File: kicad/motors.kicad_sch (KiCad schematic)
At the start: 33 parts, among them U1 DRV8251A, U15 DRV8251A, U16 DRV8251A, U17 DRV8251A, U2 DRV8251A, U3 DRV8251A

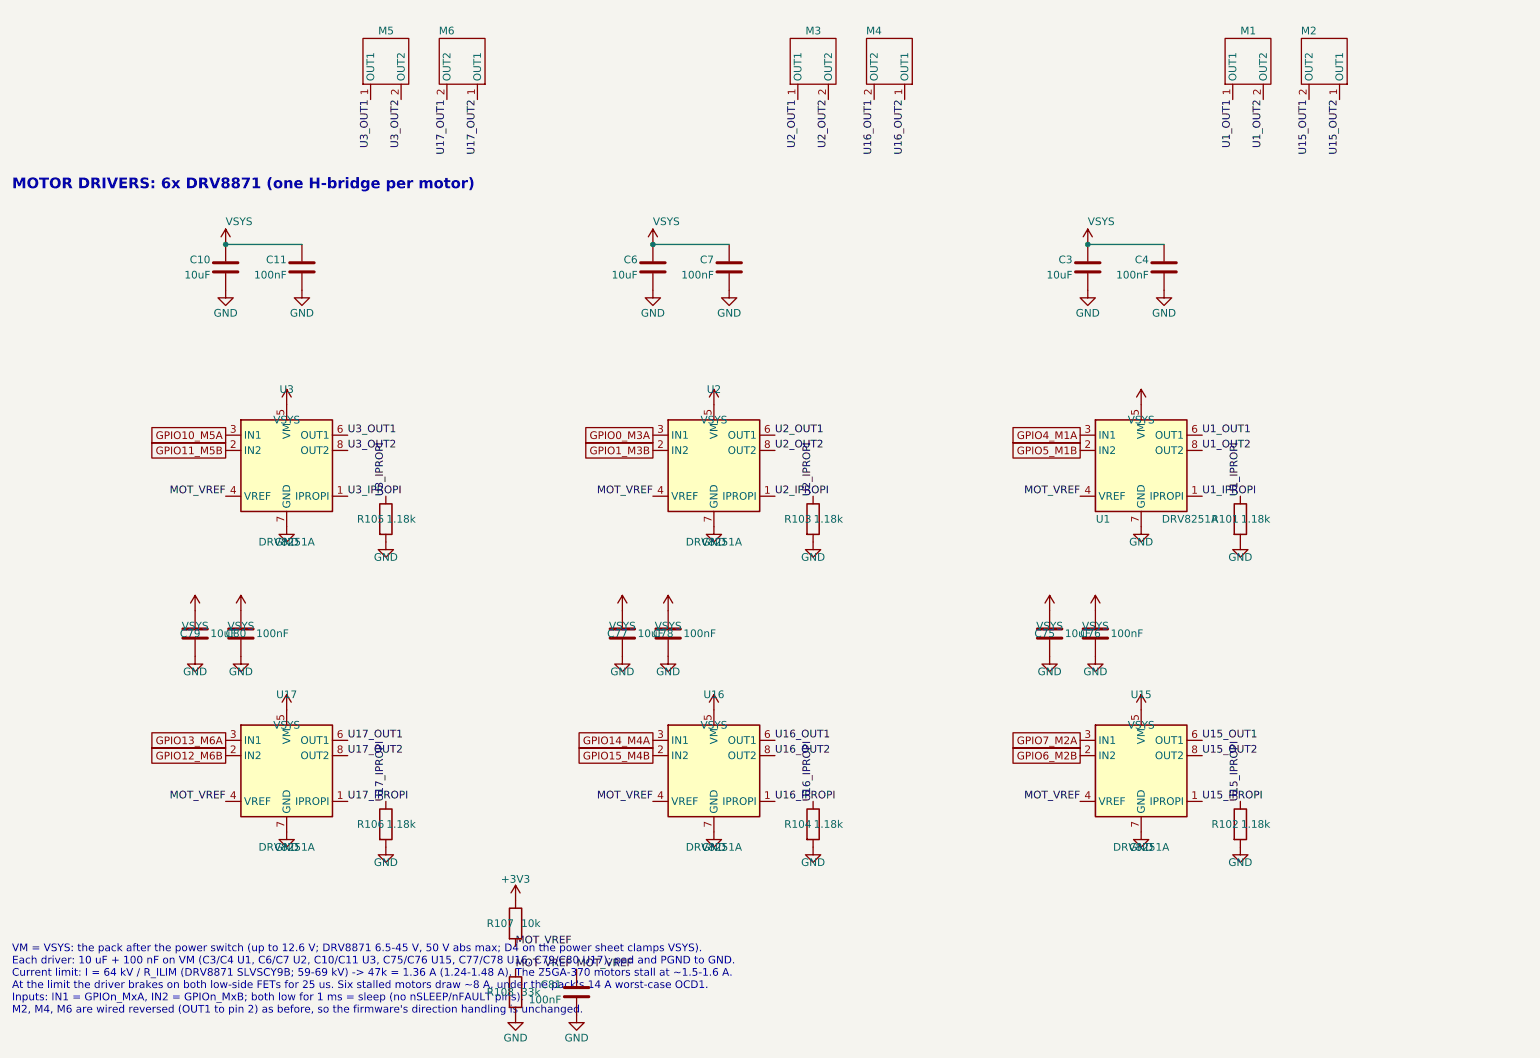
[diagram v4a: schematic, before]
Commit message: Fill in LCSC numbers, swap to stocked parts, tidy the new schematic parts
- LCSC numbers from JLC's 2026-10-19 in-stock catalog for every new part
  except the DRV8251A, which JLC doesn't stock (Global Sourcing or consign).
- 2S protector S-8252AAH -> HY2120-LB (C168778): pin-for-pin the same,
  OV 4.25 V / UV 2.80 V, stocked at JLC. R94 trip recovery still holds.
- IPROPI R101-R106 1.18k (2,341 in stock) -> 1.2k preferred (C25862),
  so the motor limit is 1.34 A.
- Fix the 2S pack board's footprint-symbol links (paths were dropped in
  the previous commit); both boards now link every footprint correctly.
- Move the VREF divider and the balancer block into clear space and
  rewrite the stale DRV8871/BQ7791501 notes on the motor and 2S sheets.

Co-Authored-By: Claude Opus 5.5 <noreply@anthropic.com>
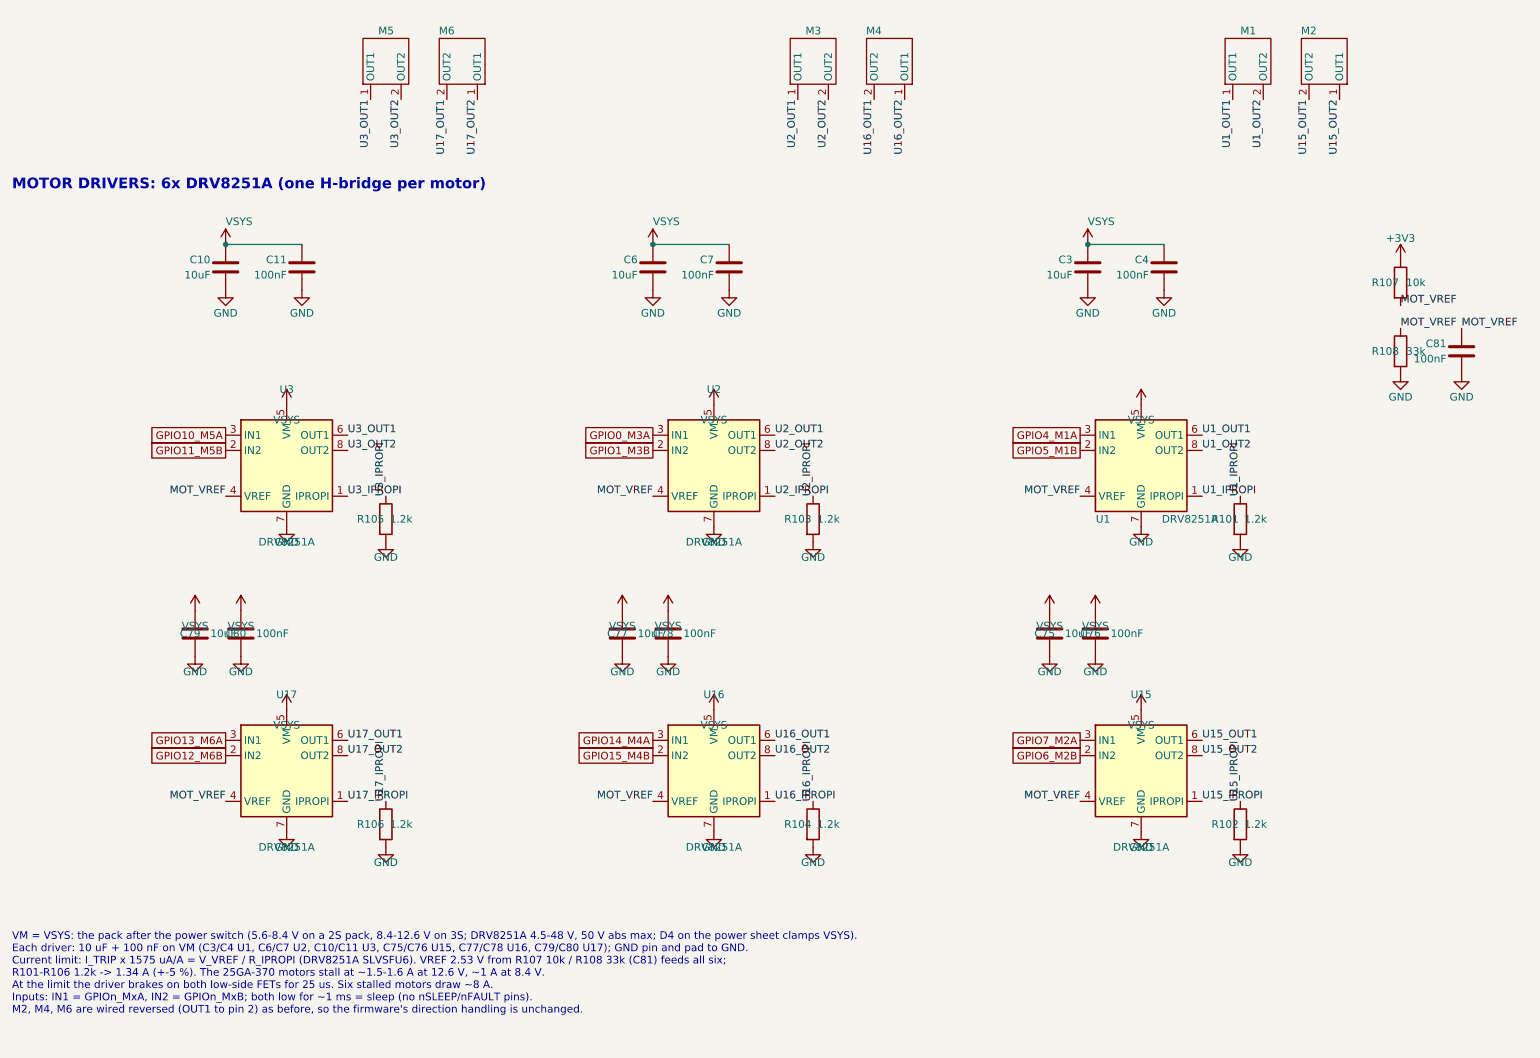
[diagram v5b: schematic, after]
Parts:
- R101, R102, R103, R104, R105, R106: value 1.18k -> 1.2k; LCSC Part # (none) -> C25862; MPN 0402WGF1181TCE -> 0402WGF1201TCE
- R108: LCSC Part # (none) -> C25779
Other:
- note added: "MOTOR DRIVERS: 6x DRV8251A (one H-bridge per motor)"
- note added: "VM = VSYS: the pack after the power switch (5.6-8.4 V on a 2S pack, 8.4-12.6 V on 3S; DRV8251A 4.5-48 V, 50 V abs max; D4 on the power sheet clamps VSYS). Each driver: 10 uF + 100 nF on VM (C3/C4 U1, C6/C7 U2, C10/C11 U3, C75/C76 U15, C77/C78 U16, C79/C80 U17); GND pin and pad to GND. Current limit: I_TRIP x 1575 uA/A = V_VREF / R_IPROPI (DRV8251A SLVSFU6). VREF 2.53 V from R107 10k / R108 33k (C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"
- note removed: "MOTOR DRIVERS: 6x DRV8871 (one H-bridge per motor)"
- note removed: "VM = VSYS: the pack after the power switch (up to 12.6 V; DRV8871 6.5-45 V, 50 V abs max; D4 on the power sheet clamps VSYS). Each driver: 10 uF + 100 nF on VM (C3/C4 U1, C6/C7 U2, C10/C11 U3, C75/C76 U15, C77/C78 U16, C79/C80 U17); pad and PGND to GND. Current limit: I = 64 kV / R_ILIM (DRV8871 SLVSCY9B; 59-69 kV) -> 47k = 1.36 A (1.24-1.48 A). The 25GA-370 motors stall at ~1.5-1.6 A. At the lim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"
- moved on the sheet: C81, R107, R108

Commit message: Give the six DRV8251As LCSC C5218844 so JLC places them
The genuine TI DRV8251ADDAR is stocked at LCSC as C5218844, so the motor
drivers no longer need Global Sourcing or consigning. fab.py now puts
U1-U3 and U15-U17 in the JLC BOM and CPL with nothing flagged.

Co-Authored-By: Claude Opus 5.5 <noreply@anthropic.com>
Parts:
- U1, U15, U16, U17, U2, U3: LCSC Part # (none) -> C5218844
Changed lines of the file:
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@@
       (effects (font (size 1.27 1.27)) (hide yes))
     )
-    (property "LCSC Part #" "" (at 215.9 88.9 0)
+    (property "LCSC Part #" "C5218844" (at 215.9 88.9 0)
       (effects (font (size 1.27 1.27)) (hide yes))
     )
@@
       (effects (font (size 1.27 1.27)) (hide yes))
     )
-    (property "LCSC Part #" "" (at 215.9 139.7 0)
+    (property "LCSC Part #" "C5218844" (at 215.9 139.7 0)
       (effects (font (size 1.27 1.27)) (hide yes))
     )
@@
       (effects (font (size 1.27 1.27)) (hide yes))
     )
-    (property "LCSC Part #" "" (at 144.78 88.9 0)
+    (property "LCSC Part #" "C5218844" (at 144.78 88.9 0)
       (effects (font (size 1.27 1.27)) (hide yes))
     )
@@
       (effects (font (size 1.27 1.27)) (hide yes))
     )
-    (property "LCSC Part #" "" (at 144.78 139.7 0)
+    (property "LCSC Part #" "C5218844" (at 144.78 139.7 0)
       (effects (font (size 1.27 1.27)) (hide yes))
     )
@@
       (effects (font (size 1.27 1.27)) (hide yes))
     )
-    (property "LCSC Part #" "" (at 73.66 88.9 0)
+    (property "LCSC Part #" "C5218844" (at 73.66 88.9 0)
       (effects (font (size 1.27 1.27)) (hide yes))
     )
@@
       (effects (font (size 1.27 1.27)) (hide yes))
     )
-    (property "LCSC Part #" "" (at 73.66 139.7 0)
-      (effects (font (size 1.27 1.27)) (hide yes))
-    )
+    (property "LCSC Part #" "C5218844" (at 73.66 139.7 0)
+      (effects (font (size 1.27 1.27)) (hide yes))
+    )

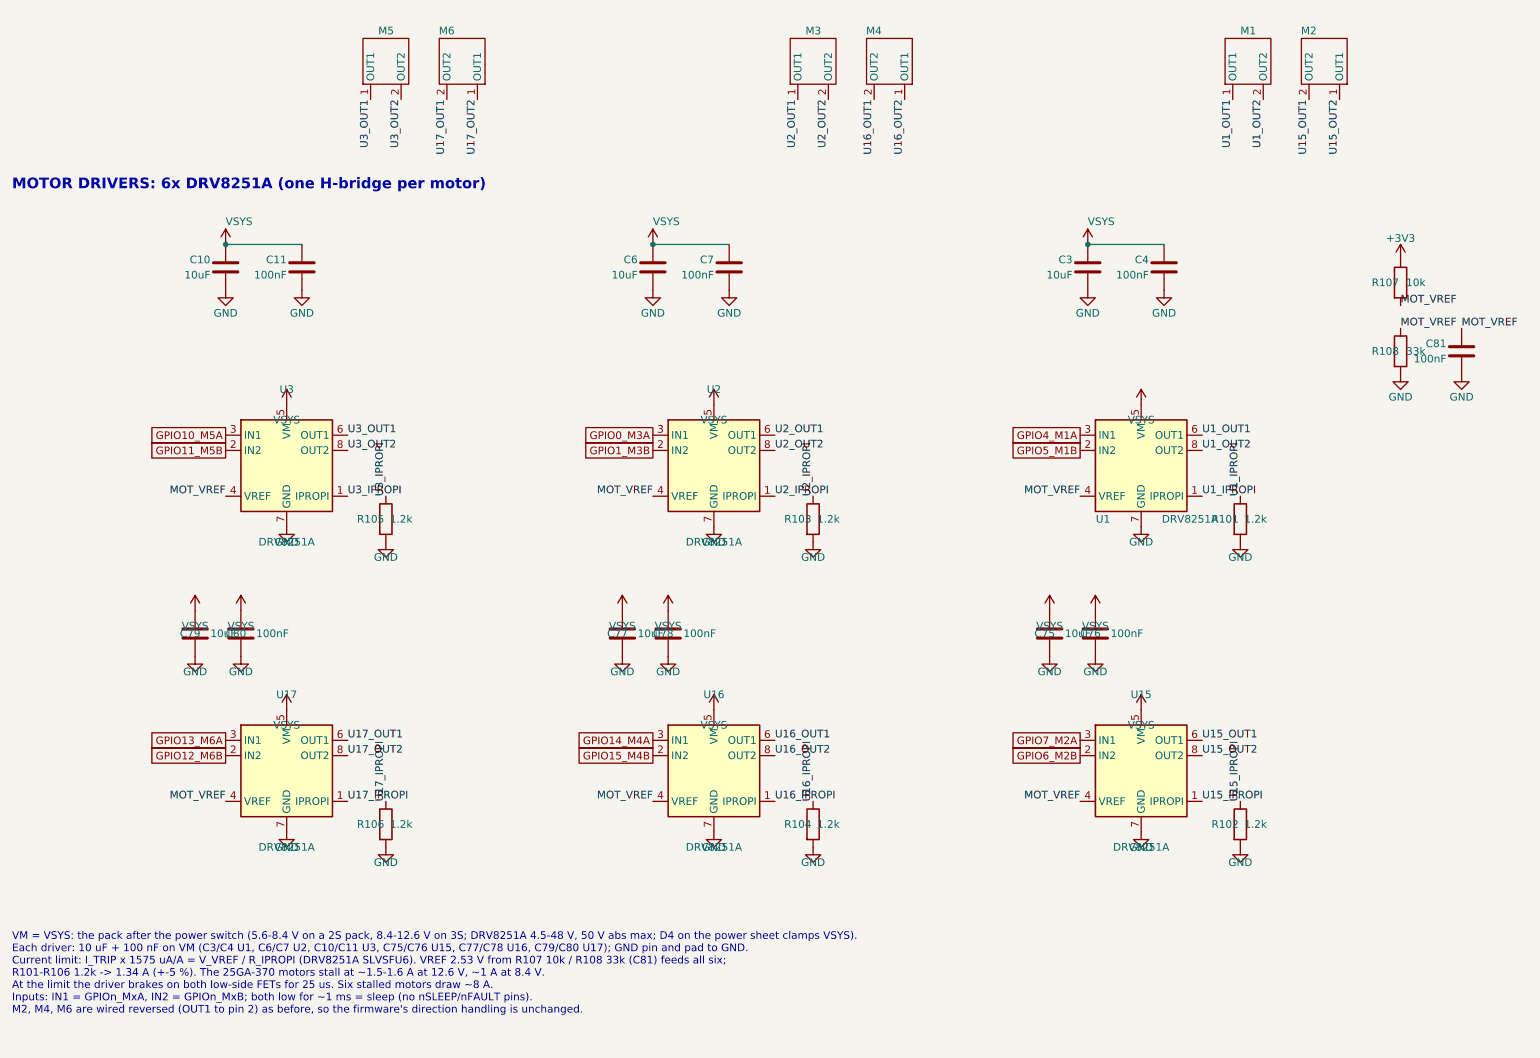
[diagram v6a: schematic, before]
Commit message: Baseline before double-sided build
The working tree as handed over: schematics, board, hexy.pretty
footprints and the new STEP models in kicad/3dmodels (now tracked
through a .gitignore exception), plus the double-sided handoff.

Co-Authored-By: Claude Opus 5.5 <noreply@anthropic.com>
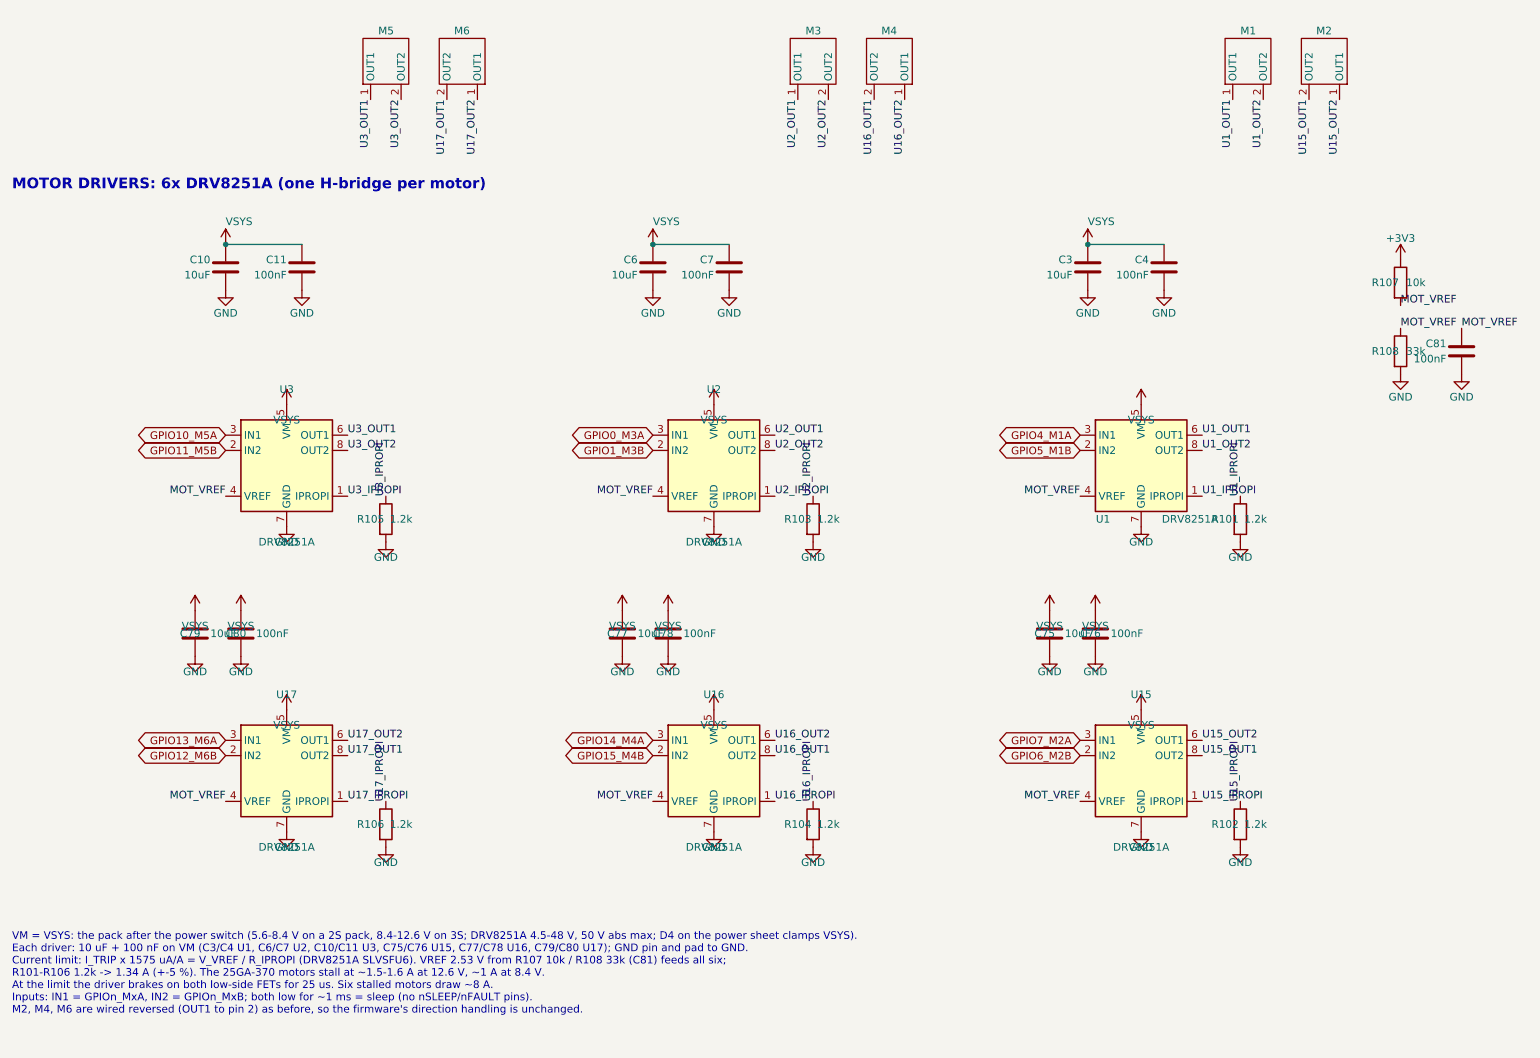
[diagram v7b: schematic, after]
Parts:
- M1, M2, M3, M4, M5, M6: value ~ -> (none)
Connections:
- net U15_OUT1: now also U15.8 (OUT2); no longer U15.6 (OUT1)
- net U15_OUT2: now also U15.6 (OUT1); no longer U15.8 (OUT2)
- net U16_OUT1: now also U16.8 (OUT2); no longer U16.6 (OUT1)
- net U16_OUT2: now also U16.6 (OUT1); no longer U16.8 (OUT2)
- net U17_OUT1: now also U17.8 (OUT2); no longer U17.6 (OUT1)
- net U17_OUT2: now also U17.6 (OUT1); no longer U17.8 (OUT2)
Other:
- moved on the sheet: M2, M4, M6
